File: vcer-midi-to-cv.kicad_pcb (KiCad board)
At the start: 4 copper layers, 140 x 128.5 mm, 106 parts, among them J1 Conn_01x10_Male, J10 CV3, J11 CV4, J12 Vel1, J13 Vel2, J14 Vel3, J15 Vel4, J16 Gate1, J17 Gate2, J18 Gate3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

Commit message: fixed mounting holes
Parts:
- removed REF**: mount_m3_hole, eurorack:mount_m3_hole
- added Mount_1: mounting, eurorack:mounting, F.Cu at (-47.5, 111.2)
- added Mount_2: mounting, eurorack:mounting, F.Cu at (-11.9, 111.2)
- added Mount_3: mounting, eurorack:mounting, F.Cu at (-47.5, -11.2)
- added Mount_4: mounting, eurorack:mounting, F.Cu at (-11.9, -11.2)
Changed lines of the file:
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@@
     (pad "" np_thru_hole circle (at 0 0) (size 2 2) (drill 2) (layers F&B.Cu *.Mask))
   )
-  (footprint "eurorack:mount_m3_hole" (layer "F.Cu")
-    (at -29.75 -11.25)
-    (attr through_hole)
-    (fp_text reference "REF**" (at -0.4 -6.1 unlocked) (layer "F.SilkS") hide
-      (effects (font (size 1 1) (thickness 0.15)))
-    )
-    (fp_text value "mount_m3_hole" (at 8.4 -0.9 unlocked) (layer "F.Fab")
-      (effects (font (size 1 1) (thickness 0.15)))
-    )
-    (fp_text user "${REFERENCE}" (at 8.4 0.6 unlocked) (layer "F.Fab")
-      (effects (font (size 1 1) (thickness 0.15)))
-    )
-    (pad "" np_thru_hole circle (at -2.51 122.5) (size 3.2 3.2) (drill 3.2) (layers F&B.Cu *.Mask))
-    (pad "" np_thru_hole circle (at -2.51 0) (size 3.2 3.2) (drill 3.2) (layers F&B.Cu *.Mask))
-  )
   (footprint "eurorack:mount_m2" (layer "F.Cu")
     (at -27.075 18.3)
@@
     )
   )
+  (footprint "eurorack:mounting" locked (layer "F.Cu")
+    (at -11.94 111.25)
+    (attr smd board_only)
+    (fp_text reference "Mount_2" (at -0.508 -8.636 unlocked) (layer "User.9") hide
+      (effects (font (size 1 1) (thickness 0.15)))
+    )
+    (fp_text value "mounting" (at 0 -7.62 unlocked) (layer "F.Fab") hide
+      (effects (font (size 1 1) (thickness 0.15)))
+    )
+    (fp_text user "Middle is 7.5mm from the left side, all other is N*5.08" (at 1.524 -4.572 unlocked) (layer "User.9") hide
+      (effects (font (size 1 1) (thickness 0.15)))
+    )
+    (fp_line (start -2.54 -1.6) (end 2.54 -1.6) (layer "Edge.Cuts") (width 0.12))
+    (fp_line (start 2.54 1.6) (end -2.54 1.6) (layer "Edge.Cuts") (width 0.12))
+    (fp_arc (start 2.54 -1.6) (mid 4.14 0) (end 2.54 1.6) (layer "Edge.Cuts") (width 0.12))
+    (fp_arc (start -2.54 1.6) (mid -4.14 0) (end -2.54 -1.6) (layer "Edge.Cuts") (width 0.12))
+    (group "" (id 3c077979-961c-40a4-b0e1-385788ffec9a)
+      (members
+        77bcca0d-c036-402f-85ac-17d648723655
+        7ba1bb98-dfa0-47e3-8e3a-850746dd2cec
+        8075a449-6cc5-42b1-a238-112c5d6f4fc6
+        874442a6-c37b-4f81-bdbd-73fe7e138cb5
+      )
+    )
+  )
   (footprint "Resistor_SMD:R_1206_3216Metric_Pad1.30x1.75mm_HandSolder" locked (layer "F.Cu")
     (at 33.6 30.4 -90)
@@
     )
   )
+  (footprint "eurorack:mounting" locked (layer "F.Cu")
+    (at -47.5 -11.25)
+    (attr smd board_only)
+    (fp_text reference "Mount_3" (at -0.252 -6.1744 unlocked) (layer "User.9") hide
+      (effects (font (size 1 1) (thickness 0.15)))
+    )
+    (fp_text value "mounting" (at 0 -7.62 unlocked) (layer "F.Fab") hide
+      (effects (font (size 1 1) (thickness 0.15)))
+    )
+    (fp_text user "Middle is 7.5mm from the left side, all other is N*5.08" (at 1.524 -4.572 unlocked) (layer "User.9") hide
+      (effects (font (size 1 1) (thickness 0.15)))
+    )
+    (fp_line (start -2.54 -1.6) (end 2.54 -1.6) (layer "Edge.Cuts") (width 0.12))
+    (fp_line (start 2.54 1.6) (end -2.54 1.6) (layer "Edge.Cuts") (width 0.12))
+    (fp_arc (start 2.54 -1.6) (mid 4.14 0) (end 2.54 1.6) (layer "Edge.Cuts") (width 0.12))
+    (fp_arc (start -2.54 1.6) (mid -4.14 0) (end -2.54 -1.6) (layer "Edge.Cuts") (width 0.12))
+    (group "" (id d2dee2f5-6152-45fc-9e8e-604eb2801b6a)
+      (members
+        4ce309b8-5b16-4637-ad05-f2ee74c02d44
+        ada33f4e-0827-4817-9dcb-58358c9182f2
+        be877774-19b9-4cf2-b0bd-508536b4d8d9
+        d5f25a1f-39df-42de-8a2c-f07613cf9db5
+      )
+    )
+  )
   (footprint "Capacitor_THT:CP_Radial_D5.0mm_P2.50mm" locked (layer "F.Cu")
     (at 70.94 80.085113 90)
@@
     )
   )
+  (footprint "eurorack:mounting" locked (layer "F.Cu")
+    (at -11.94 -11.25)
+    (attr smd board_only)
+    (fp_text reference "Mount_4" (at -0.3536 -6.1998 unlocked) (layer "User.9") hide
+      (effects (font (size 1 1) (thickness 0.15)))
+    )
+    (fp_text value "mounting" (at 0 -7.62 unlocked) (layer "F.Fab") hide
+      (effects (font (size 1 1) (thickness 0.15)))
+    )
+    (fp_text user "Middle is 7.5mm from the left side, all other is N*5.08" (at 1.524 -4.572 unlocked) (layer "User.9") hide
+      (effects (font (size 1 1) (thickness 0.15)))
+    )
+    (fp_line (start -2.54 -1.6) (end 2.54 -1.6) (layer "Edge.Cuts") (width 0.12))
+    (fp_line (start 2.54 1.6) (end -2.54 1.6) (layer "Edge.Cuts") (width 0.12))
+    (fp_arc (start -2.54 1.6) (mid -4.14 0) (end -2.54 -1.6) (layer "Edge.Cuts") (width 0.12))
+    (fp_arc (start 2.54 -1.6) (mid 4.14 0) (end 2.54 1.6) (layer "Edge.Cuts") (width 0.12))
+    (group "" (id bfaa0d22-59b3-42a6-b4cf-d6a728ba38fd)
+      (members
+        1224843a-152d-46d7-af46-8acbd1a018ba
+        2796f82f-3df9-4a5d-8777-2f11d51b0490
+        738a844e-9025-4657-8eb3-952ca12255cb
+        c7582331-c9bd-44eb-8f32-a3c02d441305
+      )
+    )
+  )
   (footprint "eurorack:logo2" (layer "F.Cu")
     (at -19.880914 89.675)
@@
     (pad "" np_thru_hole circle (at 0 0) (size 6 6) (drill 6) (layers F&B.Cu *.Mask))
   )
+  (footprint "eurorack:mounting" locked (layer "F.Cu")
+    (at -47.5 111.25)
+    (attr smd board_only)
+    (fp_text reference "Mount_1" (at -0.508 -8.636 unlocked) (layer "User.9") hide
+      (effects (font (size 1 1) (thickness 0.15)))
+    )
+    (fp_text value "mounting" (at 0 -7.62 unlocked) (layer "F.Fab") hide
+      (effects (font (size 1 1) (thickness 0.15)))
+    )
+    (fp_text user "Middle is 7.5mm from the left side, all other is N*5.08" (at 1.524 -4.572 unlocked) (layer "User.9") hide
+      (effects (font (size 1 1) (thickness 0.15)))
+    )
+    (fp_line (start -2.54 -1.6) (end 2.54 -1.6) (layer "Edge.Cuts") (width 0.12))
+    (fp_line (start 2.54 1.6) (end -2.54 1.6) (layer "Edge.Cuts") (width 0.12))
+    (fp_arc (start -2.54 1.6) (mid -4.14 0) (end -2.54 -1.6) (layer "Edge.Cuts") (width 0.12))
+    (fp_arc (start 2.54 -1.6) (mid 4.14 0) (end 2.54 1.6) (layer "Edge.Cuts") (width 0.12))
+    (group "" (id 4b8db379-ee9b-41ff-81f1-3c6a7bdb2844)
+      (members
+        484e5e8f-43db-4180-b2d1-ca2468e9d868
+        7e89c0e8-2bca-4b78-a0e9-9e7bab2a3a9f
+        a178344c-93a7-4199-9876-146cd45d1ec4
+        f9669737-a1d7-4c80-8946-9a5470d32ab4
+      )
+    )
+  )
   (footprint "Resistor_SMD:R_1206_3216Metric_Pad1.30x1.75mm_HandSolder" locked (layer "F.Cu")
     (at 49.6225 63.8 -90)
@@
   (gr_line locked (start 45 100) (end 85 100) (layer "Edge.Cuts") (width 0.2))
   (gr_line locked (start 85 2.5) (end 45 2.5) (layer "User.8") (width 0.15))
-  (gr_line (start -55 -11.25) (end -4.5 -11.25) (layer "User.8") (width 0.15))
   (gr_line locked (start 47.475 0.05) (end 47.475 100.05) (layer "User.8") (width 0.15))
-  (gr_line (start -55 111.25) (end -4.5 111.25) (layer "User.8") (width 0.15))
   (gr_line locked (start 82.475 100.05) (end 82.475 0.05) (layer "User.8") (width 0.15))
   (gr_line locked (start 40 99.5) (end 0 99.5) (layer "User.9") (width 0.15))
@@
     (effects (font (size 0.5 0.5) (thickness 0.125)) (justify mirror))
   )
-  (gr_text "JLCJLCJLCJLC" (at -47.905914 -12.1) (layer "B.SilkS")
+  (gr_text "JLCJLCJLCJLC" (at -47.5488 -8.0772) (layer "B.SilkS")
     (effects (font (size 1 1) (thickness 0.15)) (justify mirror))
   )
@@
     (effects (font (size 1 1) (thickness 0.15)))
   )
-  (gr_text "MIDI" (at -12.280914 109.525) (layer "F.SilkS")
+  (gr_text "MIDI" (at -21.5392 111.3028) (layer "F.SilkS")
     (effects (font (size 3 3) (thickness 0.3)))
   )

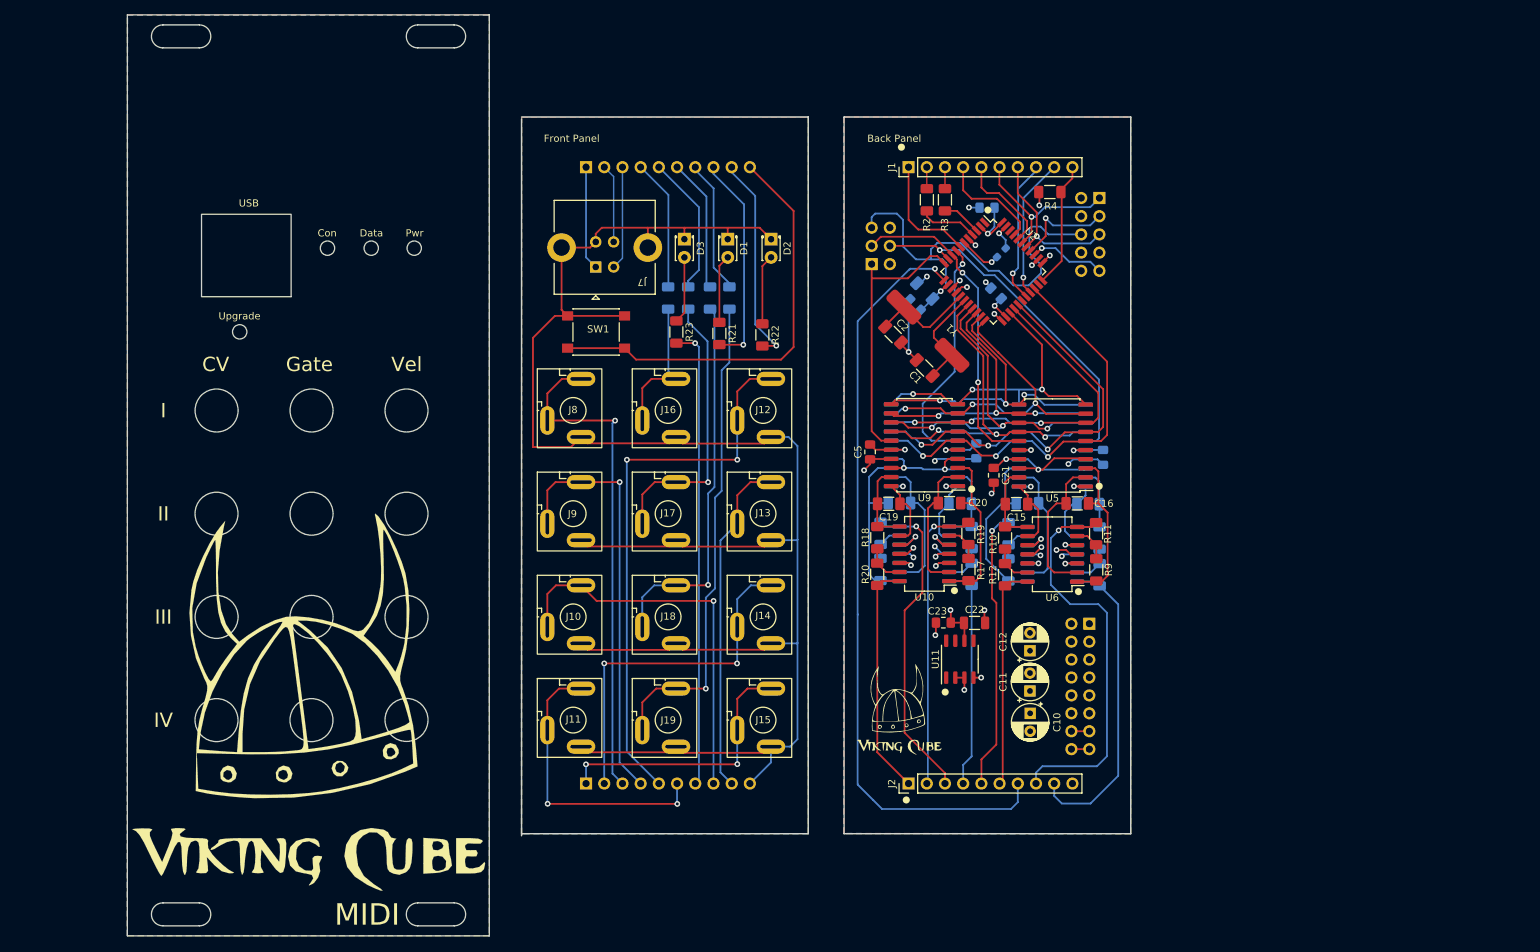
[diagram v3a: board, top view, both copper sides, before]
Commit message: removed other panels
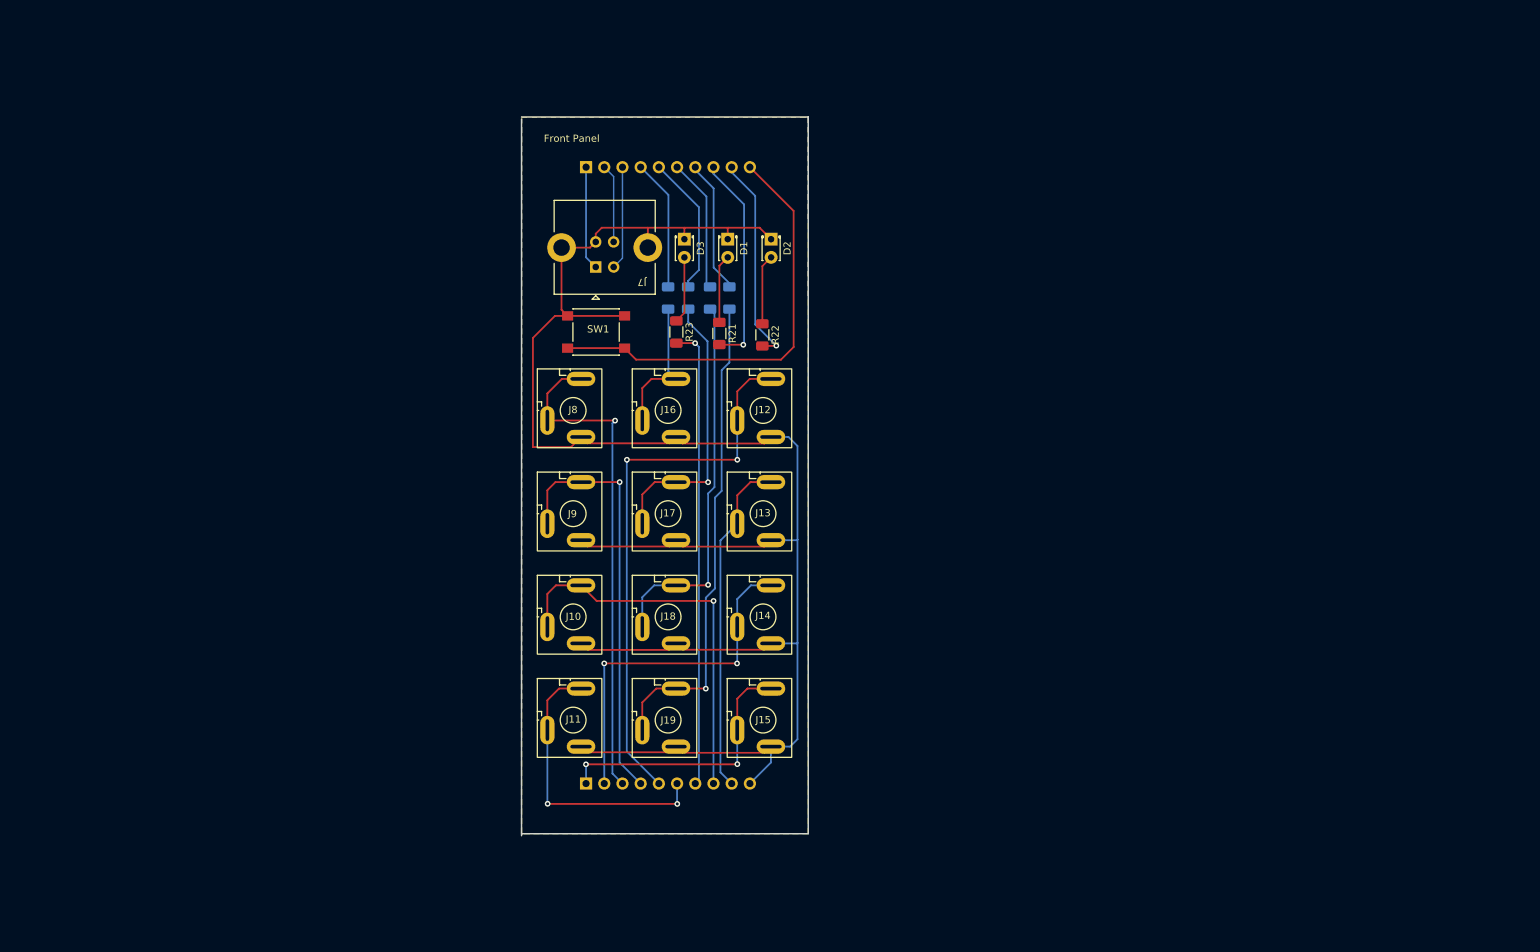
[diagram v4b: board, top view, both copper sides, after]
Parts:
- removed C1, C2: 18pF, Capacitor_SMD:C_1206_3216Metric_Pad1.33x1.80mm_HandSolder
- removed C10, C11, C12: 100uF, Capacitor_THT:CP_Radial_D5.0mm_P2.50mm
- removed C13, C14, C15, C16, C17, C18, C19, C20: 15pF, Capacitor_SMD:C_1206_3216Metric_Pad1.33x1.80mm_HandSolder
- removed C21, C3, C5, C6, C7, C8, C9: 100nF, Capacitor_SMD:C_0805_2012Metric_Pad1.18x1.45mm_HandSolder
- removed C22: 1uF (TANT), Capacitor_SMD:C_1206_3216Metric
- removed C23: 100nF (Ceramic), Capacitor_SMD:C_0805_2012Metric_Pad1.18x1.45mm_HandSolder
- removed C4: 1u, Capacitor_SMD:C_0603_1608Metric_Pad1.08x0.95mm_HandSolder
- removed the G*** at (55.0, 84.6)
- removed the G*** at (-19.9, 89.7)
- removed J1, J2: Conn_01x10_Male, Connector_PinHeader_2.54mm:PinHeader_1x10_P2.54mm_Vertical
- removed J5: AVR-ISP-6, Connector_PinHeader_2.54mm:PinHeader_2x03_P2.54mm_Vertical
- removed J6: AVR-JTAG-10, Connector_PinHeader_2.54mm:PinHeader_2x05_P2.54mm_Vertical
- removed Mount_1, Mount_2, Mount_3, Mount_4: mounting, eurorack:mounting
- removed R1, R4: 10k, Resistor_SMD:R_1206_3216Metric_Pad1.30x1.75mm_HandSolder
- removed R10, R11, R12, R13, R14, R15, R16, R17, R18, R19, R20, R5, R6, R7, R8, R9: R-10k-1206, Resistor_SMD:R_1206_3216Metric_Pad1.30x1.75mm_HandSolder
- removed R2, R3: 22, Resistor_SMD:R_1206_3216Metric_Pad1.30x1.75mm_HandSolder
- removed REF1, REF10, REF11, REF12, REF2, REF3, REF4, REF5, REF6, REF7, REF8, REF9: mount_LUM_1502-03, eurorack:mount_LUM_1502-03
- removed REF13, REF14, REF15, REF16: mount_m2, eurorack:mount_m2
- removed REF17: mount_USB-BG, eurorack:mount_USB-BG
- removed U1: power_conn_16, eurorack:power_16
- removed U10, U4, U6, U8: TL074, Package_SO:SO-14_5.3x10.2mm_P1.27mm
- removed U11: REF195, Package_SO:SO-8_3.9x4.9mm_P1.27mm
- removed U2: ATmega32U4-A, Package_QFP:TQFP-44_10x10mm_P0.8mm
- removed U3, U5, U7, U9: TLC7528, Package_SO:SOIC-20W_7.5x12.8mm_P1.27mm
- removed Y1: 16Mhz, eurorack:HC49-4HSMX
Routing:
- net GND: track 393.7 -> 0.00 mm, vias 28 -> 0
- net +5V: track 296.0 -> 0.00 mm, vias 10 -> 0
- net /L3: track 107.4 -> 0.00 mm, vias 1 -> 0
- net +5F: track 82.8 -> 0.00 mm, vias 4 -> 0
- net +12V: track 77.9 -> 0.00 mm, vias 5 -> 0
- net -12V: track 64.3 -> 0.00 mm, vias 4 -> 0
- net /reset: track 61.7 -> 0.00 mm, vias 1 -> 0
- net /DACA/B: track 60.5 -> 0.00 mm, vias 3 -> 0
- net /D7: track 57.0 -> 0.00 mm, vias 3 -> 0
- net /CV3: track 55.5 -> 0.00 mm, vias 1 -> 0
- net /D0: track 50.3 -> 0.00 mm, vias 3 -> 0
- net /D6: track 49.8 -> 0.00 mm, vias 3 -> 0
- net /D1: track 48.9 -> 0.00 mm, vias 3 -> 0
- net /CS3: track 48.9 -> 0.00 mm, vias 1 -> 0
- net /D5: track 45.2 -> 0.00 mm, vias 3 -> 0
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- removed copper zone on B.Cu, net (none)
- removed copper zone on F.Cu, net (none)
- removed copper zone on B.Cu, net GND
- removed copper zone on F.Cu, net GND
- removed copper zone on In1.Cu, net GND
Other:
- board size 140 x 128.5 mm -> 40 x 100.3 mm
- board text removed: "+12V"
- board text removed: "+45;0"
- board text removed: "+5V"
- board text removed: "-12V"
- board text removed: "-55;0 [-50] 10HP"
- board text removed: "Back Panel"
- board text removed: "CV"
- board text removed: "Con"
- board text removed: "Data"
- board text removed: "GND"
- board text removed: "Gate"
- board text removed: "I"
- board text removed: "II"
- board text removed: "III"
- board text removed: "ISP"
- board text removed: "IV"
- board text removed: "JLCJLCJLCJLC"
- board text removed: "JTAG"
- board text removed: "MIDI"
- board text removed: "NC"
- board text removed: "Pwr"
- board text removed: "RED"
- board text removed: "USB"
- board text removed: "Upgrade"
- board text removed: "Vel"
